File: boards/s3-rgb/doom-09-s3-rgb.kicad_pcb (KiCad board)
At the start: 4 copper layers, 182 x 80 mm, 85 parts, among them J1 54132-4062, J2 S2B-PH-K-S(LF)(SN), J5 S2B-PH-K-S(LF)(SN), J6 S2B-PH-K-S(LF)(SN), U1 ESP32-S3-WROOM-1-N16R8, U2 IP5306, U3 MCP23017-E/SO, U4 PCM5102APWR, U5 PAM8403DR, U6 AMS1117-3.3, U7 ESD 2-line, U8 MT3608

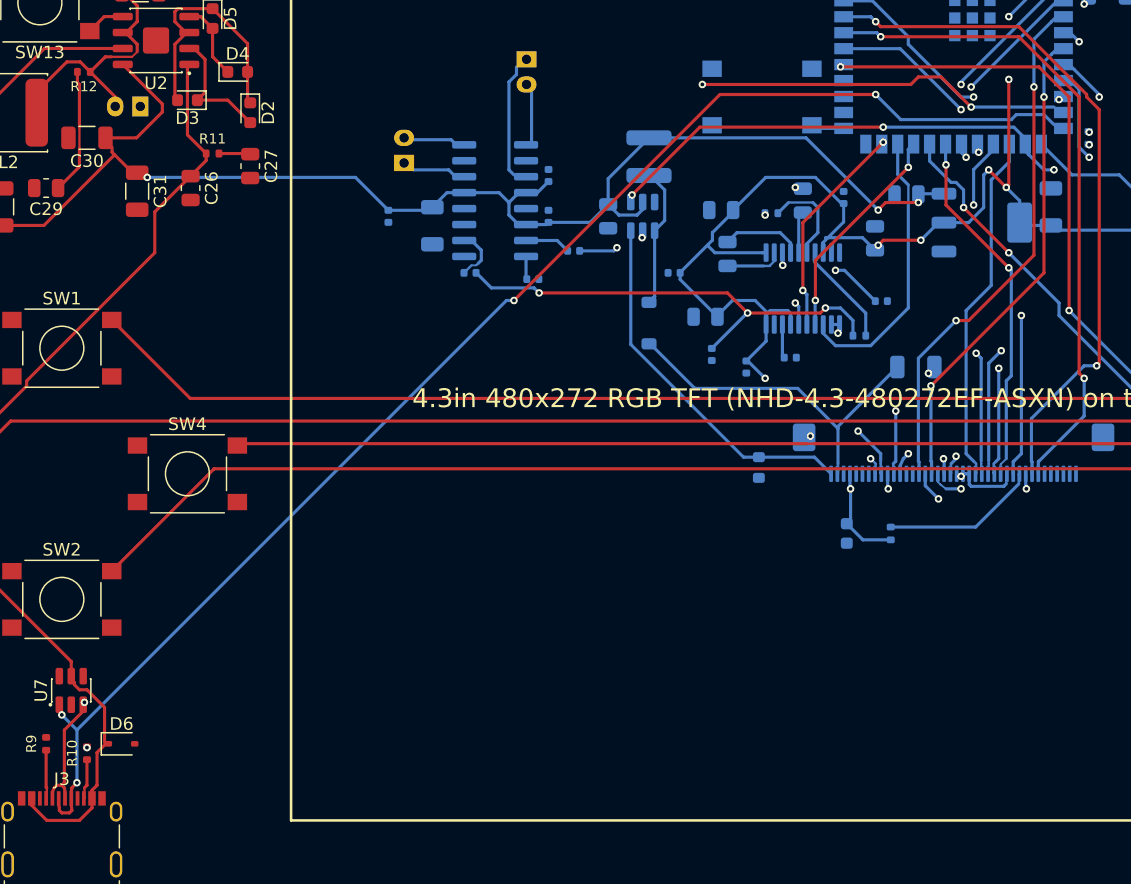
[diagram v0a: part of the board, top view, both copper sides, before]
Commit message: PCBKit's mark and pcbkit.io on every board; the RP2350 handheld ready to order
The handheld runs from two 18650 cells in parallel behind a DW01A protector and a reverse-cell
P-MOSFET, charged at up to 500 mA from the Pico's USB-C by a BQ24075 (power path into VSYS, timers
off for 6 Ah), with an on/off switch on 3V3_EN, M3 holes, ground pours and the console on pads.
Every assembled part has a JLCPCB code in stock (Basic where there is one); the module sockets are
in the BOM, the modules listed in the order's README. Check complete, the ready review clean.
Every board: routed and checked complete with the new mark.
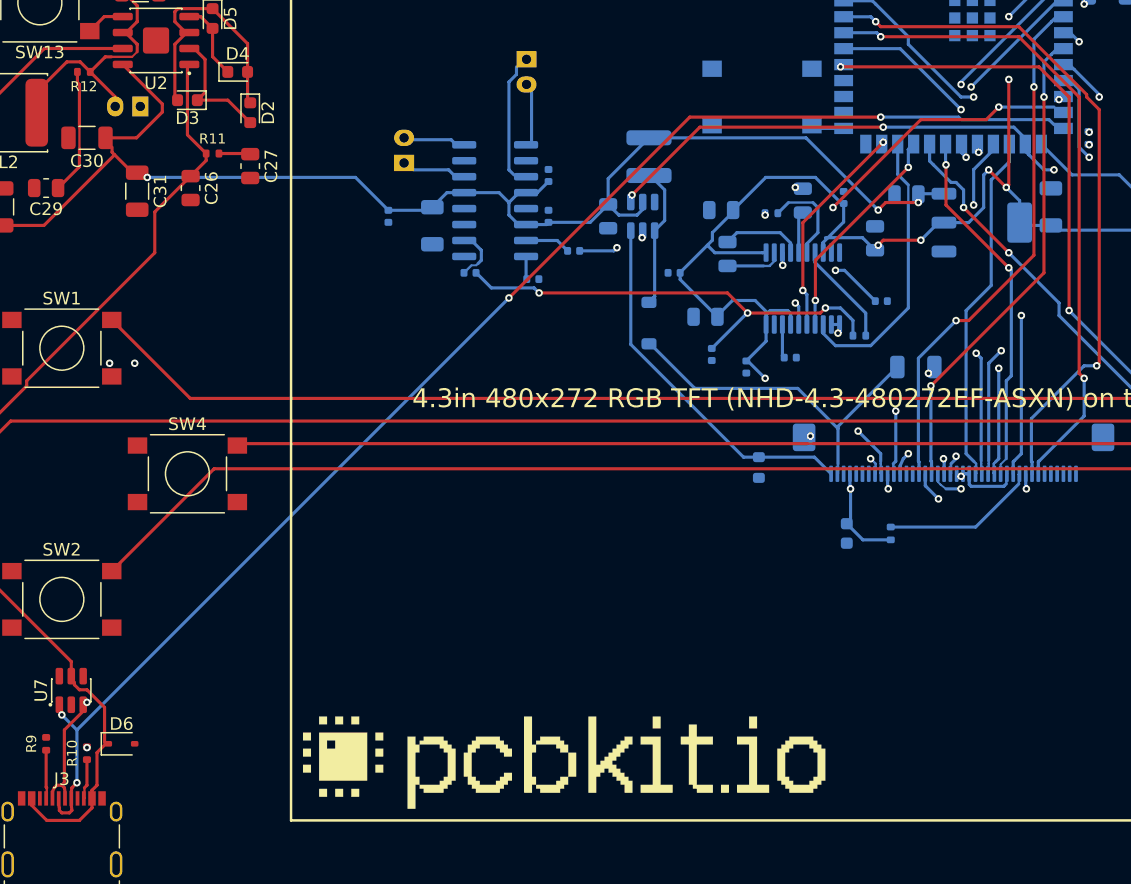
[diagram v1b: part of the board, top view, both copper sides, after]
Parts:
- added logo: , Logo_PCBKit_pcbkit.io, F.Cu at (160.0, 189.0)
- SW1, SW10, SW11, SW12, SW13, SW2, SW3, SW4, SW5, SW6, SW7, SW8, SW9: value (none) -> PTS645SM43SMTR92 LFS
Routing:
- net DN: track 106.9 -> 104.9 mm
- net DP: track 109.0 -> 107.2 mm
- net GND: vias 12 -> 14

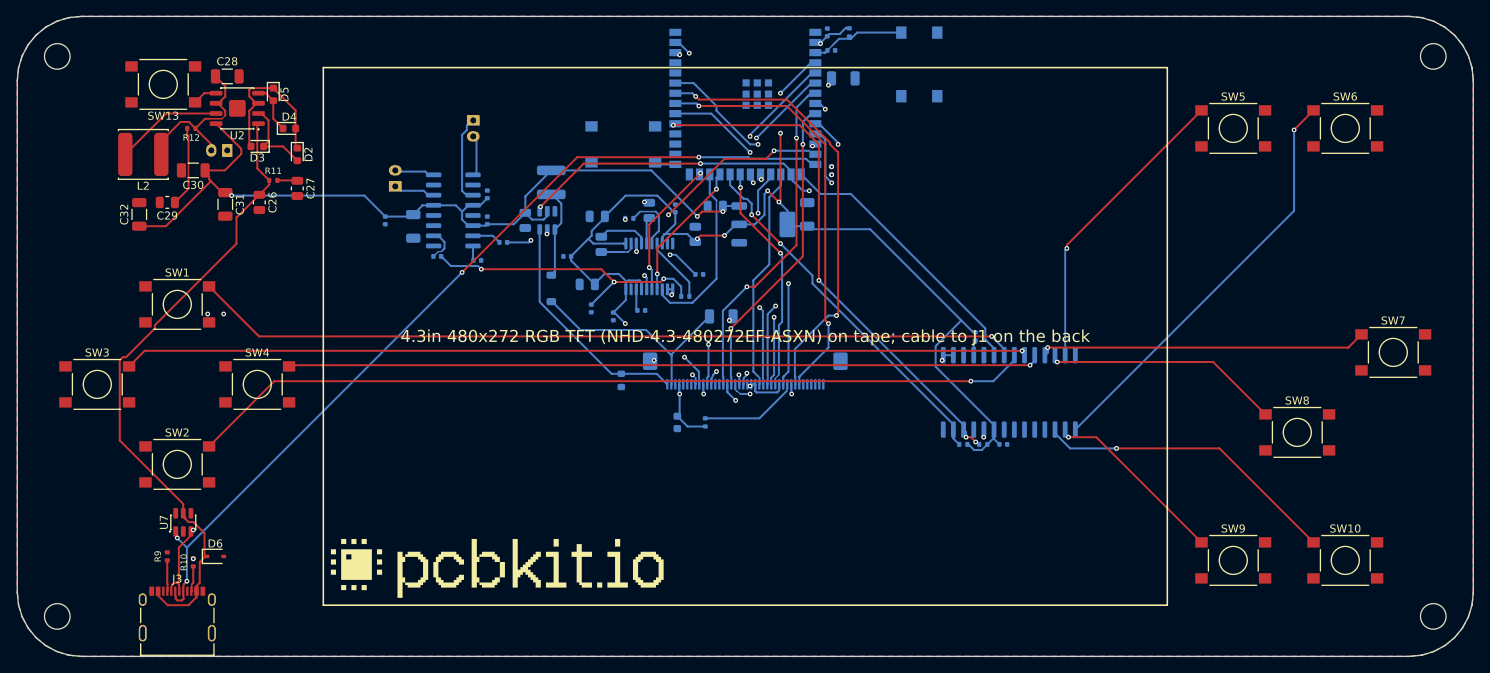
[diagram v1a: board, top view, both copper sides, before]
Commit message: s3-rgb: two 18650 cells with protection and a USB-C charger; panel clear of through-hole pins
The IP5306 power bank, its LiPo plug and the AMS1117 become two 18650 in parallel (Keystone 1042
holders end to end along the back's bottom edge) behind a reverse-cell P-FET and DW01A + FS8205A,
a BQ24075 power path from the USB-C port (fuse, TVS, ESD), and a TLV75533 low-dropout 3.3 V
regulator with the on/off switch on its EN; the backlight boost and the amplifier run from SYS.
The panel's FFC connector moves to the top edge on the back (its cable folds over the edge) and
the speaker plugs to the left and right edges, clear of the taped panel. Every assembled part
pinned to an in-stock LCSC code; the README says how to charge, flash and assemble.
check: complete, 0 errors, 1 warning (USB pair coupling, justified); ready lens: nothing to fix;
fab export without --force.

Claude-Session: https://claude.ai/code/session_01ATmMmxyrWxFwR3nTdXUrcx
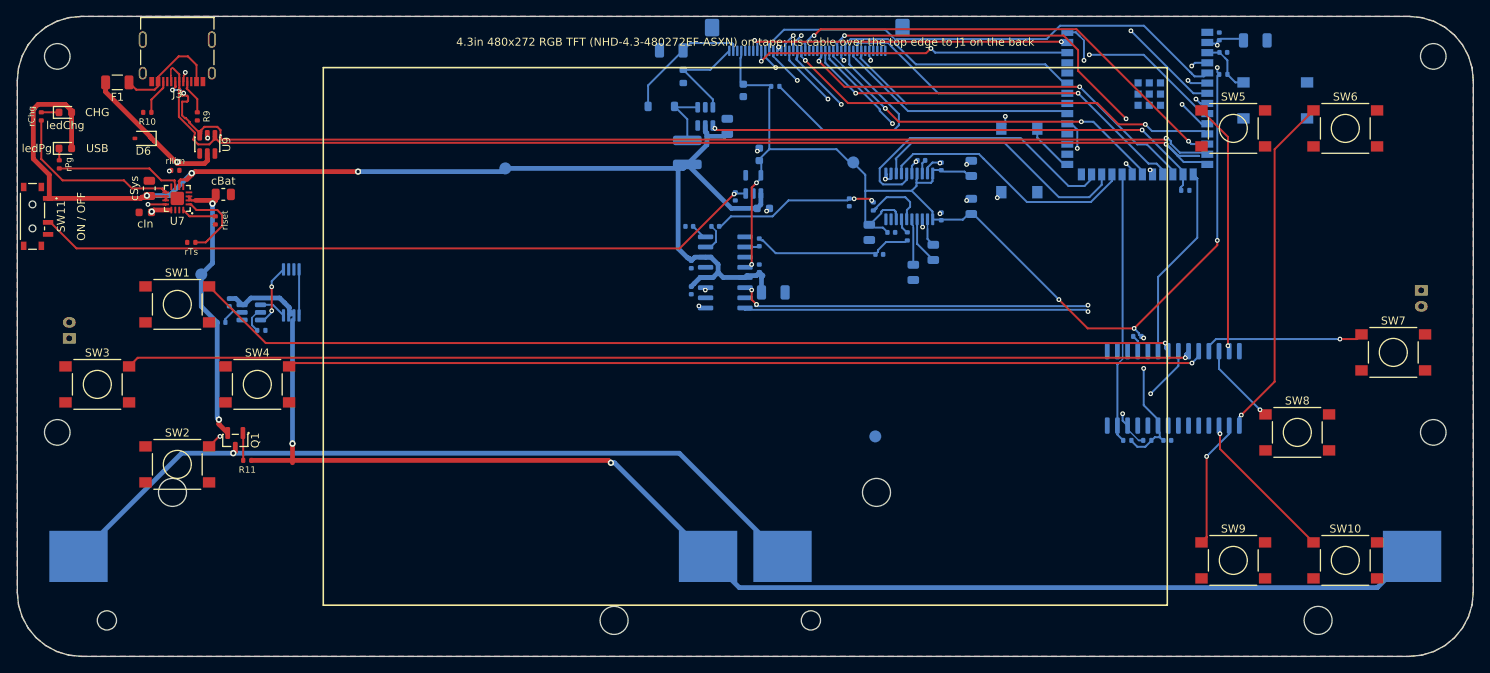
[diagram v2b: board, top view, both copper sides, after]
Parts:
- removed C27, C29: 10uF, C_0805_2012Metric
- removed C28, C30, C31, C32: 22uF, C_1206_3216Metric
- removed D2, D3, D4, D5: blue, LED_0603_1608Metric
- removed J2: S2B-PH-K-S(LF)(SN), JST_PH_S2B-PH-K_1x02_P2.00mm_Horizontal
- removed L2: 1uH, L_Power_6x6mm
- added BT1: 1042, BatteryHolder_Keystone_1042_1x18650, B.Cu at (147.0, 187.5)
- added BT2: 1042, BatteryHolder_Keystone_1042_1x18650, B.Cu at (235.0, 187.5)
- added DS1 (x4): NHD-4.3-480272EF-ASXN#, Newhaven_NHD-4.3-480272EF_Panel, F.Cu at (191.0, 160.0)
- added F1: PTC 1000mA, Fuse_1206_3216Metric, F.Cu at (112.5, 128.2)
- added Q1: AO3401A, SOT-23, F.Cu at (127.2, 173.0)
- added Q2: FS8205A, TSSOP-8_4.4x2.93mm_P0.65mm, B.Cu at (134.2, 154.5)
- added R13: 1kohm, R_0402_1005Metric, B.Cu at (130.5, 159.2)
- added R14: 100kohm, R_0402_1005Metric, B.Cu at (189.8, 142.5)
- added U9: ESD 2-line, SOT-23-6, F.Cu at (123.8, 136.0)
- added cBat: 4.7uF, C_0805_2012Metric, F.Cu at (125.8, 142.2)
- added cIn: 1uF, C_0603_1608Metric, F.Cu at (116.0, 144.5)
- added cSys: 4.7uF, C_0805_2012Metric, F.Cu at (116.5, 141.5)
- added ledChg: red, LED_0603_1608Metric, F.Cu at (106.0, 132.0)
- added ledPg: green, LED_0603_1608Metric, F.Cu at (106.0, 136.5)
- added rChg: 1.5kohm, R_0402_1005Metric, F.Cu at (103.0, 132.5)
- added rIlim: 1.18kohm, R_0402_1005Metric, F.Cu at (119.8, 139.2)
- added rIset: 1.13kohm, R_0402_1005Metric, F.Cu at (124.8, 145.5)
- added rPg: 1.5kohm, R_0402_1005Metric, F.Cu at (105.2, 138.5)
- added rTs: 10kohm, R_0402_1005Metric, F.Cu at (121.8, 148.2)
- added tpBat: , TestPoint_Round_D1.5mm, B.Cu at (123.0, 152.2)
- added tpGnd: , TestPoint_Round_D1.5mm, B.Cu at (207.2, 172.5)
- added tpSys: , TestPoint_Round_D1.5mm, B.Cu at (161.0, 139.0)
- added tpV3: , TestPoint_Round_D1.5mm, B.Cu at (204.5, 138.2)
- C26: value 10uF -> 100nF; footprint C_0805_2012Metric -> C_0402_1005Metric; moved to B.Cu
- C33: value 10uF -> 1uF; footprint C_0805_2012Metric -> C_0603_1608Metric
- C34: value 22uF -> 1uF; footprint C_1206_3216Metric -> C_0603_1608Metric
- D1: value schottky -> 1N5819HW-7-F
- R11: value 2ohm -> 100kohm
- R12: value 2ohm -> 100ohm; moved to B.Cu
- SW11: value PTS645SM43SMTR92 LFS -> MSK12C02; footprint SW_Tactile_SPST_6x6mm_SMD -> SW_Slide_SPDT_Shouhan_MSK12C02; moved to F.Cu
- SW13, logo: moved to B.Cu
- U2: value IP5306 -> DW01A; footprint SOIC-8-1EP_3.9x4.9mm_P1.27mm_EP2.09x2.09mm -> SOT-6_1.6x2.9mm_P0.95mm; moved to B.Cu
- U6: value AMS1117-3.3 -> TLV75533PDBVR; footprint SOT-223 -> SOT-23-5
- U7: value ESD 2-line -> BQ24075RGTR; footprint SOT-23-6 -> QFN-16-1EP_3x3mm_P0.5mm_EP1.68x1.68mm
- moved J6 129.1 mm to (275.5, 155.2), turned to 90 degrees
- moved SW11 112.5 mm to (101.9, 145.0)
- moved SW13 107.4 mm to (225.2, 138.0), turned to 270 degrees
- moved SW12 81.7 mm to (257.2, 130.5), turned to 0 degrees
- moved J3 63.7 mm to (120.0, 128.2), turned to 180 degrees
- moved R10 56.5 mm to (116.2, 132.0), turned to 180 degrees
- moved J5 56.5 mm to (106.5, 159.2), turned to 270 degrees
- moved R9 55.1 mm to (122.5, 132.5), turned to 270 degrees
- moved D6 53.0 mm to (115.8, 135.2), turned to 180 degrees
- moved C4 51.7 mm to (254.8, 123.0)
- moved C13 50.1 mm to (219.2, 139.0), turned to 270 degrees
- moved C5 49.0 mm to (250.2, 122.5)
- moved C6 49.0 mm to (250.8, 124.5)
- moved U1 49.0 mm to (240.0, 127.2)
- moved R3 47.0 mm to (250.8, 127.2), turned to 180 degrees
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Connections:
- net Net-(C15-1) renamed DAC_VNEG
- net Net-(C16-1) renamed DAC_1V8
- C19 pad 1: V5 -> SYS
- C2 pad 1: V5 -> SYS
- C20 pad 1: V5 -> SYS
- C21 pad 1: V5 -> SYS
- C22 pad 1: V5 -> SYS
- C24 pad 1: Net-(C24-1) -> LINE_L
- C24 pad 2: LINE_L -> Net-(C24-1)
- C26 pad 1: VBUS -> CELL_N
- C26 pad 2: GND -> Net-(C26-1)
- C33 pad 1: V5 -> SYS
- J3 pad A4: VBUS -> usb/power/raw
- J3 pad B4: VBUS -> usb/power/raw
- L1 pad 1: V5 -> SYS
- R11 pad 1: VBUS -> CELL_N
- R11 pad 2: U2Support/C6_P -> reversed/gate
- R12 pad 1: VBAT -> BAT
- R12 pad 2: U2Support/C7_P -> Net-(C26-1)
- R3 pad 1: EN -> V3
- R3 pad 2: V3 -> EN
- R7 pad 1: Net-(R7-1) -> LINE_L
- R7 pad 2: LINE_L -> Net-(R7-1)
- SW11 pad 1: EN -> SYS
- SW11 pad 2: EN -> LDO_EN
- SW12 pad 1: Net-(SW12-1) -> EN
- SW12 pad 2: Net-(SW12-1) -> EN
- U1 pad 27: Net-(SW12-1) -> Net-(SW13-1)
- U2 pad 1: VBUS -> Net-(Q2-4)
- U2 pad 2: GAUGE1 -> Net-(R13-1)
- U2 pad 3: GAUGE2 -> Net-(Q2-5)
- U2 pad 4: GAUGE3 -> (no net)
- U2 pad 5: Net-(SW13-1) -> Net-(C26-1)
- U2 pad 6: VBAT -> CELL_N
- U5 pad 12: (no net) -> V3
- U5 pad 13: V5 -> SYS
- U5 pad 4: V5 -> SYS
- U5 pad 6: V5 -> SYS
- U6 pad 1: GND -> SYS
- U6 pad 2: V3 -> GND
- U6 pad 3: V5 -> LDO_EN
- U6 pad 4: V3 -> (no net)
- U7 pad 1: DP -> TS
- U7 pad 2: GND -> BAT
- U7 pad 3: DN -> BAT
- U7 pad 4: (no net) -> GND
- U7 pad 5: VBUS -> GND
- U7 pad 6: (no net) -> SYS
- U8 pad 5: V5 -> SYS
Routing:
- net CELL_N: track 0.00 -> 180.4 mm, vias 0 -> 2
- net SYS: track 0.00 -> 163.4 mm, vias 0 -> 3
- net V5: track 105.0 -> 0.00 mm, vias 3 -> 0
- net BAT_IN: track 0.00 -> 98.7 mm, vias 0 -> 1
- net LDO_EN: track 0.00 -> 91.3 mm, vias 0 -> 1
- net SPK_RP: track 3.28 -> 90.1 mm, vias 0 -> 1
- net SPK_RN: track 3.37 -> 87.2 mm, vias 0 -> 3
- net SPK_LP: track 4.00 -> 83.8 mm, vias 0 -> 1
- net SPK_LN: track 9.01 -> 83.7 mm, vias 0 -> 1
- net VBUS: track 78.0 -> 28.9 mm, vias 0 -> 2
- net DP: track 107.2 -> 149.3 mm, vias 4 -> 1
- net DN: track 104.9 -> 144.7 mm, vias 3 -> 4
- net BAT: track 0.00 -> 35.2 mm, vias 0 -> 2
- net VSYNC: track 55.4 -> 29.7 mm, vias 2 -> 0
- net UP: track 103.4 -> 128.2 mm
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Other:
- board text added: "+"
- board text added: "-"
- board text added: "2 x 18650 Li-ion 3.7 V"
- board text added: "4.3in 480x272 RGB TFT (NHD-4.3-480272EF-ASXN) on tape; its cable over the top edge to J1 on the back"
- board text added: "CHG"
- board text added: "ON / OFF"
- board text added: "USB"
- board text removed: "4.3in 480x272 RGB TFT (NHD-4.3-480272EF-ASXN) on tape; cable to J1 on the back"
